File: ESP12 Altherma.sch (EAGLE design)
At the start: 53 parts, among them CON1 PGM/BT Serial, CON2 X85A - PL, CON3 X10A, CON5 Thermo Rly, K1 HRS1KH-S_DC5V, K2 HRS1KH-S_DC5V, U1 TLP291-4, U2 AP2112K-3.3, U4 DRDC3105E6-7, U5 SN74LVC1G125GV

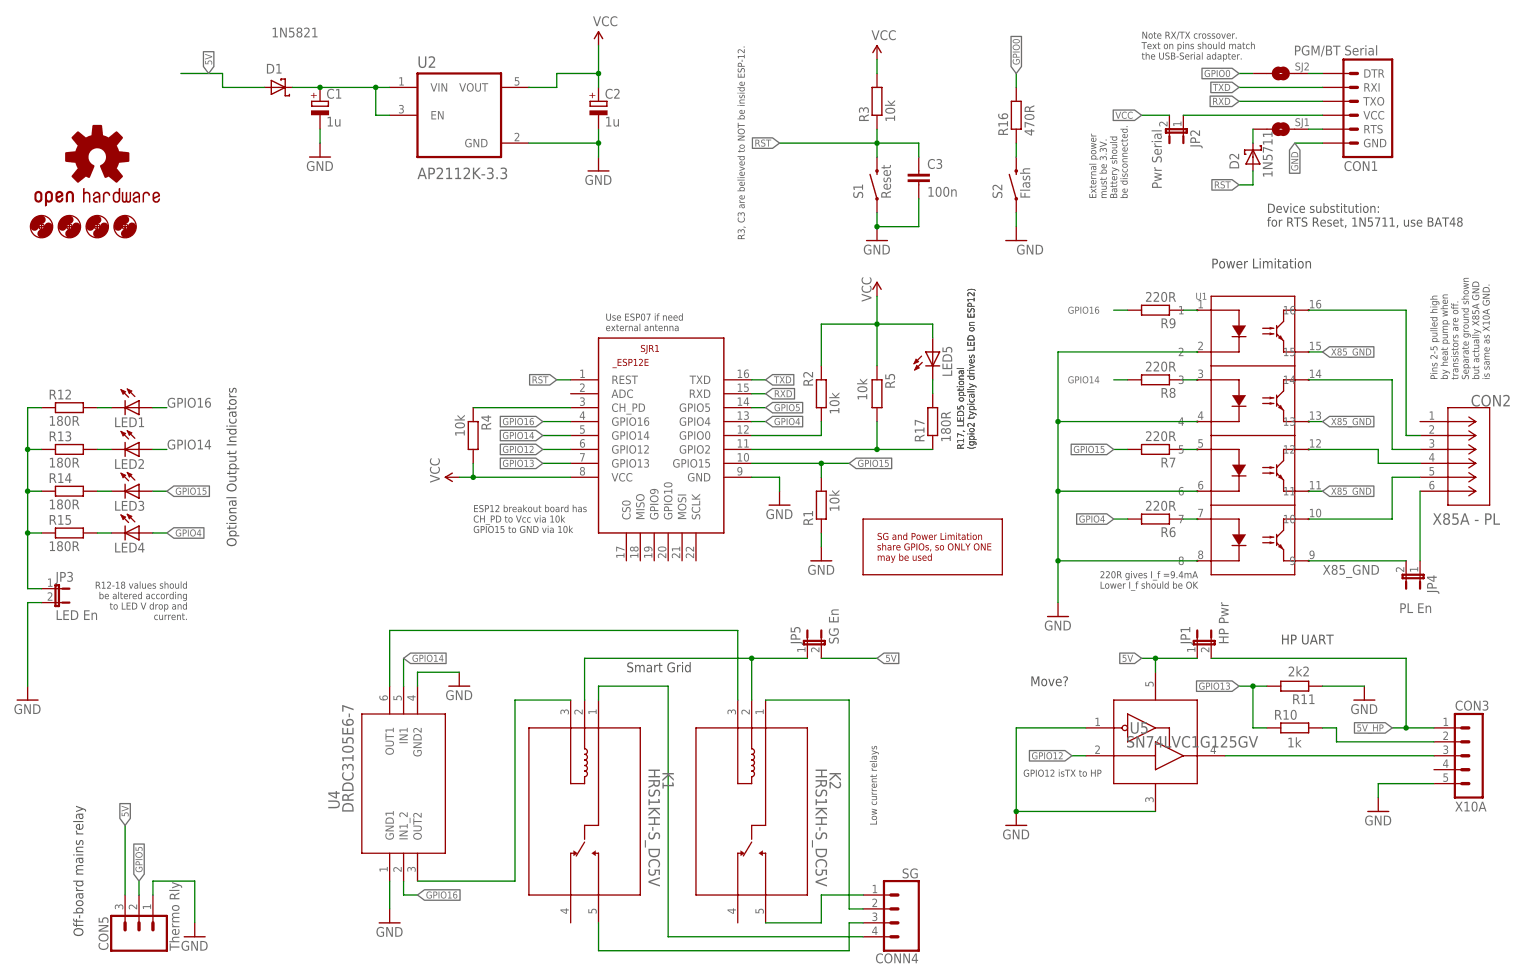
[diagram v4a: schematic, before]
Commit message: clean up schematic
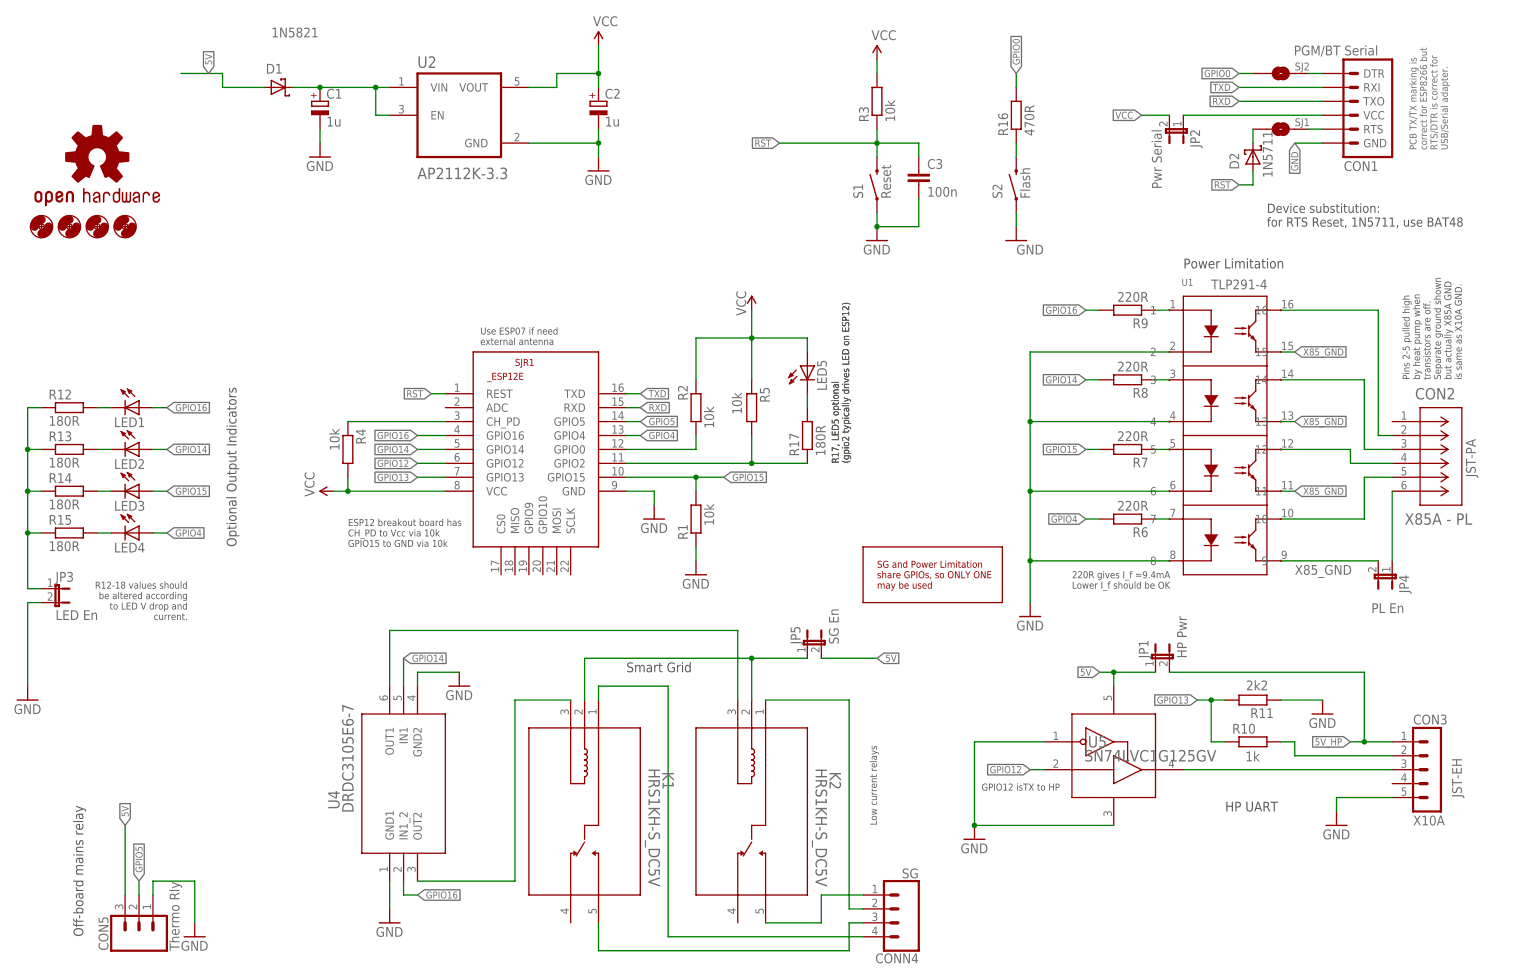
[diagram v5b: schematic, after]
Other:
- note added: "JST-EH"
- note added: "JST-PA"
- note added: "PCB TX/TX marking is correct for ESP8266 but RTS/DTR is correct for USB/Serial adapter."
- note added: "TLP291-4"
- note removed: "External power must be 3.3V. Battery should be disconnected."
- note removed: "Move?"
- note removed: "Note RX/TX crossover. Text on pins should match the USB-Serial adapter."
- note removed: "R3, C3 are believed to NOT be inside ESP-12."
- moved on the sheet: CON2, CON3, JP1, JP4, LED5, R1, R10, R11, R17, R2, R4, R5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
